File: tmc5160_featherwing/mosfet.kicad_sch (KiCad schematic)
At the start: 2 parts, among them U2 BUK7D36-60EX

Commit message: Add connectors
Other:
- company: (none) -> Howard Hughes Medical Institute
- title: (none) -> tmc5160_featherwing
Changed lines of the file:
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@@
 (kicad_sch (version 20230121) (generator eeschema)
   (paper "A4")
+  (title_block
+    (title "tmc5160_featherwing")
+    (date "2024-03-25")
+    (rev "1.0")
+    (company "Howard Hughes Medical Institute")
+  )
   (junction (at 152.4 69.85) (diameter 0) (color 0 0 0 0)
   )

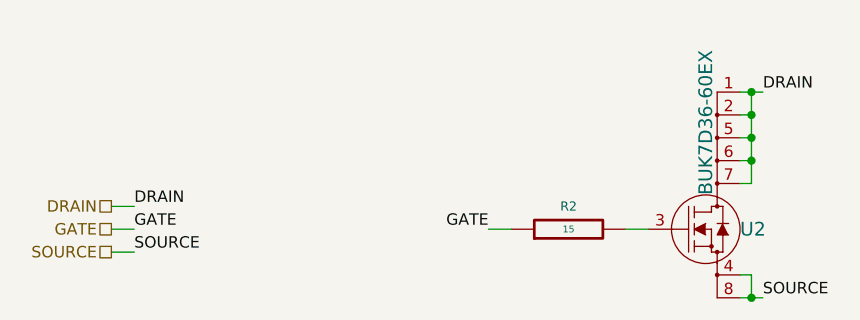
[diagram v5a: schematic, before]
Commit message: Add capacitors and resistors
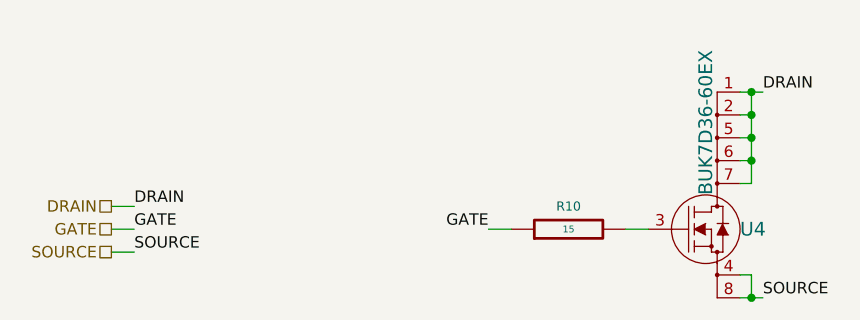
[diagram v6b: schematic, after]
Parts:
- removed R2: 15, Janelia:R_0402_1005Metric, symbol Janelia:R_15_0402
- added R10: 15, Janelia:R_0402_1005Metric, symbol Janelia:R_15_0.1W_0402
- renumbered U2 to U4
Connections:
- net GATE: now also R10.1
- net at U4.3 (G): now also R10.2
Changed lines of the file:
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@@
   (title_block
     (title "tmc5160_featherwing")
-    (date "2024-04-11")
+    (date "2024-04-12")
     (rev "1.0")
     (company "Howard Hughes Medical Institute")
@@
     (effects (font (size 1.27 1.27)) (justify right))
   )
-  (symbol (lib_id "Janelia:R_15_0402") (at 132.08 80.01 90) (unit 1)
-    (in_bom yes) (on_board yes) (dnp no)
-    (property "Reference" "R2" (at 132.08 77.47 90)
-      (effects (font (size 1.016 1.016)))
-    )
-    (property "Value" "15" (at 132.08 80.01 90) (do_not_autoplace)
-      (effects (font (size 0.762 0.762)))
-    )
-    (property "Footprint" "Janelia:R_0402_1005Metric" (at 132.08 81.788 90)
-      (effects (font (size 0.762 0.762)) hide)
-    )
-    (property "Datasheet" "" (at 132.08 77.978 90)
-      (effects (font (size 0.762 0.762)))
-    )
-    (property "Vendor" "Digi-Key" (at 129.54 75.438 90)
-      (effects (font (size 1.524 1.524)) hide)
-    )
-    (property "Vendor Part Number" "P15.0LCT-ND" (at 127 72.898 90)
-      (effects (font (size 1.524 1.524)) hide)
-    )
-    (property "Description" "RES SMD 15 OHM 1% 1/10W" (at 124.46 70.358 90)
-      (effects (font (size 1.524 1.524)) hide)
-    )
-    (property "Package" "0402" (at 132.08 80.01 0)
-      (effects (font (size 1.27 1.27)) hide)
-    )
-    (property "Manufacturer" "Panasonic Electronic Components" (at 132.08 80.01 0)
-      (effects (font (size 1.27 1.27)) hide)
-    )
-    (property "Manufacturer Part Number" "ERJ-2RKF15R0X" (at 132.08 80.01 0)
-      (effects (font (size 1.27 1.27)) hide)
-    )
-    (pin "1")
-    (pin "2")
-    (instances
-      (project "tmc5160_featherwing"
-        (path "/df2b2e89-e055-4140-95de-f1df723db034/039ac378-5273-4081-85bf-9eb26cb5ed57/77ec754f-e73d-4b40-8cb6-04aa79ed075b"
-          (reference "R2") (unit 1)
-        )
-        (path "/df2b2e89-e055-4140-95de-f1df723db034/039ac378-5273-4081-85bf-9eb26cb5ed57/3a5be366-e07c-4cea-9d17-ab6873df58d0"
-          (reference "R3") (unit 1)
-        )
-        (path "/df2b2e89-e055-4140-95de-f1df723db034/039ac378-5273-4081-85bf-9eb26cb5ed57/015fc9e7-3ba8-423b-8c7a-1e6ac6af06ca"
-          (reference "R4") (unit 1)
-        )
-        (path "/df2b2e89-e055-4140-95de-f1df723db034/039ac378-5273-4081-85bf-9eb26cb5ed57/310c6d75-c755-45f6-91bd-c6a3e28c41c3"
-          (reference "R5") (unit 1)
-        )
-        (path "/df2b2e89-e055-4140-95de-f1df723db034/039ac378-5273-4081-85bf-9eb26cb5ed57/e5ac0a82-cfa0-413a-a1a3-5e88ae5fe4fa"
-          (reference "R6") (unit 1)
-        )
-        (path "/df2b2e89-e055-4140-95de-f1df723db034/039ac378-5273-4081-85bf-9eb26cb5ed57/33c1e78d-612d-4de4-b4ab-c1f2402fd86d"
-          (reference "R7") (unit 1)
-        )
-        (path "/df2b2e89-e055-4140-95de-f1df723db034/039ac378-5273-4081-85bf-9eb26cb5ed57/3cc889de-698d-4e8a-bf98-2840b1fad77e"
-          (reference "R8") (unit 1)
-        )
-        (path "/df2b2e89-e055-4140-95de-f1df723db034/039ac378-5273-4081-85bf-9eb26cb5ed57/166b4ba4-5822-49d8-b309-f52ce04f60b1"
-          (reference "R1") (unit 1)
-        )
-      )
-    )
-  )
   (symbol (lib_id "Janelia:BUK7D36-60EX") (at 147.32 80.01 0) (unit 1)
     (in_bom yes) (on_board yes) (dnp no) (fields_autoplaced)
-    (property "Reference" "U2" (at 151.13 80.01 0) (do_not_autoplace)
+    (property "Reference" "U4" (at 151.13 80.01 0) (do_not_autoplace)
       (effects (font (size 1.524 1.524)) (justify left))
     )
@@
       (project "tmc5160_featherwing"
         (path "/df2b2e89-e055-4140-95de-f1df723db034/039ac378-5273-4081-85bf-9eb26cb5ed57/166b4ba4-5822-49d8-b309-f52ce04f60b1"
-          (reference "U2") (unit 1)
+          (reference "U4") (unit 1)
         )
         (path "/df2b2e89-e055-4140-95de-f1df723db034/039ac378-5273-4081-85bf-9eb26cb5ed57/77ec754f-e73d-4b40-8cb6-04aa79ed075b"
-          (reference "U3") (unit 1)
+          (reference "U5") (unit 1)
         )
         (path "/df2b2e89-e055-4140-95de-f1df723db034/039ac378-5273-4081-85bf-9eb26cb5ed57/3a5be366-e07c-4cea-9d17-ab6873df58d0"
-          (reference "U4") (unit 1)
+          (reference "U6") (unit 1)
         )
         (path "/df2b2e89-e055-4140-95de-f1df723db034/039ac378-5273-4081-85bf-9eb26cb5ed57/015fc9e7-3ba8-423b-8c7a-1e6ac6af06ca"
-          (reference "U5") (unit 1)
+          (reference "U7") (unit 1)
         )
         (path "/df2b2e89-e055-4140-95de-f1df723db034/039ac378-5273-4081-85bf-9eb26cb5ed57/310c6d75-c755-45f6-91bd-c6a3e28c41c3"
-          (reference "U6") (unit 1)
+          (reference "U8") (unit 1)
         )
         (path "/df2b2e89-e055-4140-95de-f1df723db034/039ac378-5273-4081-85bf-9eb26cb5ed57/e5ac0a82-cfa0-413a-a1a3-5e88ae5fe4fa"
-          (reference "U7") (unit 1)
+          (reference "U9") (unit 1)
         )
         (path "/df2b2e89-e055-4140-95de-f1df723db034/039ac378-5273-4081-85bf-9eb26cb5ed57/33c1e78d-612d-4de4-b4ab-c1f2402fd86d"
-          (reference "U8") (unit 1)
+          (reference "U10") (unit 1)
         )
         (path "/df2b2e89-e055-4140-95de-f1df723db034/039ac378-5273-4081-85bf-9eb26cb5ed57/3cc889de-698d-4e8a-bf98-2840b1fad77e"
-          (reference "U9") (unit 1)
+          (reference "U11") (unit 1)
         )
       )
+    )
+  )
+  (symbol (lib_id "Janelia:R_15_0.1W_0402") (at 132.08 80.01 90) (unit 1)
+    (in_bom yes) (on_board yes) (dnp no)
+    (property "Reference" "R10" (at 132.08 77.47 90)
+      (effects (font (size 1.016 1.016)))
+    )
+    (property "Value" "15" (at 132.08 80.01 90) (do_not_autoplace)
+      (effects (font (size 0.762 0.762)))
+    )
+    (property "Footprint" "Janelia:R_0402_1005Metric" (at 132.08 81.788 90)
+      (effects (font (size 0.762 0.762)) hide)
+    )
+    (property "Datasheet" "" (at 132.08 77.978 90)
+      (effects (font (size 0.762 0.762)))
+    )
+    (property "Vendor" "Digi-Key" (at 129.54 75.438 90)
+      (effects (font (size 1.524 1.524)) hide)
+    )
+    (property "Vendor Part Number" "P15.0LCT-ND" (at 127 72.898 90)
+      (effects (font (size 1.524 1.524)) hide)
+    )
+    (property "Description" "RES SMD 15 OHM 1% 1/10W" (at 124.46 70.358 90)
+      (effects (font (size 1.524 1.524)) hide)
+    )
+    (property "Package" "0402" (at 132.08 80.01 0)
+      (effects (font (size 1.27 1.27)) hide)
+    )
+    (property "Manufacturer" "Panasonic Electronic Components" (at 132.08 80.01 0)
+      (effects (font (size 1.27 1.27)) hide)
+    )
+    (property "Manufacturer Part Number" "ERJ-2RKF15R0X" (at 132.08 80.01 0)
+      (effects (font (size 1.27 1.27)) hide)
+    )
+    (pin "2")
+    (pin "1")
+    (instances
+      (project "tmc5160_featherwing"
+        (path "/df2b2e89-e055-4140-95de-f1df723db034/039ac378-5273-4081-85bf-9eb26cb5ed57/166b4ba4-5822-49d8-b309-f52ce04f60b1"
+          (reference "R10") (unit 1)
+        )
+        (path "/df2b2e89-e055-4140-95de-f1df723db034/039ac378-5273-4081-85bf-9eb26cb5ed57/77ec754f-e73d-4b40-8cb6-04aa79ed075b"
+          (reference "R11") (unit 1)
+        )
+        (path "/df2b2e89-e055-4140-95de-f1df723db034/039ac378-5273-4081-85bf-9eb26cb5ed57/3a5be366-e07c-4cea-9d17-ab6873df58d0"
+          (reference "R12") (unit 1)
+        )
+        (path "/df2b2e89-e055-4140-95de-f1df723db034/039ac378-5273-4081-85bf-9eb26cb5ed57/015fc9e7-3ba8-423b-8c7a-1e6ac6af06ca"
+          (reference "R13") (unit 1)
+        )
+        (path "/df2b2e89-e055-4140-95de-f1df723db034/039ac378-5273-4081-85bf-9eb26cb5ed57/310c6d75-c755-45f6-91bd-c6a3e28c41c3"
+          (reference "R14") (unit 1)
+        )
+        (path "/df2b2e89-e055-4140-95de-f1df723db034/039ac378-5273-4081-85bf-9eb26cb5ed57/e5ac0a82-cfa0-413a-a1a3-5e88ae5fe4fa"
+          (reference "R15") (unit 1)
+        )
+        (path "/df2b2e89-e055-4140-95de-f1df723db034/039ac378-5273-4081-85bf-9eb26cb5ed57/33c1e78d-612d-4de4-b4ab-c1f2402fd86d"
+          (reference "R16") (unit 1)
+        )
+        (path "/df2b2e89-e055-4140-95de-f1df723db034/039ac378-5273-4081-85bf-9eb26cb5ed57/3cc889de-698d-4e8a-bf98-2840b1fad77e"
+          (reference "R17") (unit 1)
+        )
+      )
